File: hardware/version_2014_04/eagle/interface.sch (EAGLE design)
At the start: 19 parts

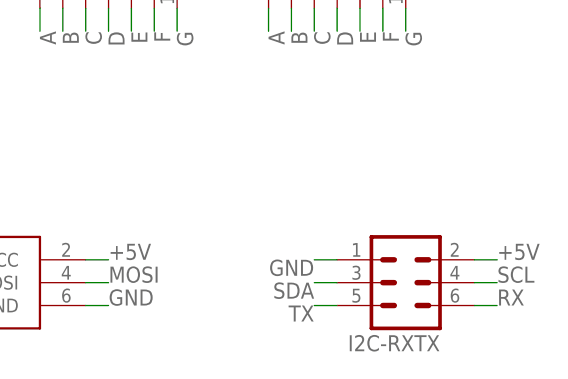
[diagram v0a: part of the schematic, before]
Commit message: mirrored RXTX connector
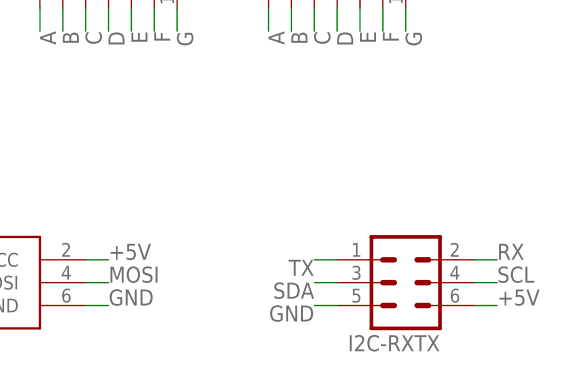
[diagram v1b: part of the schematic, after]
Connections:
- net +5V: now also I2C-RXTX.6; no longer I2C-RXTX.2
- net GND: now also I2C-RXTX.5; no longer I2C-RXTX.1
- net RX: now also I2C-RXTX.2; no longer I2C-RXTX.6
- net TX: now also I2C-RXTX.1; no longer I2C-RXTX.5
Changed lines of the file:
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@@
-</segment>
-<segment>
-<pinref part="I2C-RXTX" gate="1" pin="1"/>
-<wire x1="190.5" y1="15.24" x2="187.96" y2="15.24" width="0.1524" layer="91"/>
-<label x="187.96" y="15.24" size="1.778" layer="95" rot="R180"/>
 </segment>
 <segment>
@@
 <pinref part="C1" gate="G$1" pin="2"/>
 <pinref part="GND3" gate="1" pin="GND"/>
+</segment>
+<segment>
+<pinref part="I2C-RXTX" gate="1" pin="5"/>
+<wire x1="190.5" y1="10.16" x2="187.96" y2="10.16" width="0.1524" layer="91"/>
+<label x="187.96" y="10.16" size="1.778" layer="95" rot="R180"/>
 </segment>
 </net>
@@
 </segment>
 <segment>
-<pinref part="I2C-RXTX" gate="1" pin="2"/>
-<wire x1="205.74" y1="15.24" x2="208.28" y2="15.24" width="0.1524" layer="91"/>
-<label x="208.28" y="15.24" size="1.778" layer="95"/>
-</segment>
-<segment>
 <pinref part="ISP" gate="G$1" pin="VCC"/>
 <wire x1="162.56" y1="15.24" x2="165.1" y2="15.24" width="0.1524" layer="91"/>
@@
 <label x="-15.24" y="68.58" size="1.778" layer="95"/>
 </segment>
+<segment>
+<pinref part="I2C-RXTX" gate="1" pin="6"/>
+<wire x1="205.74" y1="10.16" x2="208.28" y2="10.16" width="0.1524" layer="91"/>
+<label x="208.28" y="10.16" size="1.778" layer="95"/>
+</segment>
 </net>
 <net name="A" class="0">
@@
 </segment>
 <segment>
-<pinref part="I2C-RXTX" gate="1" pin="6"/>
-<wire x1="205.74" y1="10.16" x2="208.28" y2="10.16" width="0.1524" layer="91"/>
-<label x="208.28" y="10.16" size="1.778" layer="95"/>
+<pinref part="I2C-RXTX" gate="1" pin="2"/>
+<wire x1="205.74" y1="15.24" x2="208.28" y2="15.24" width="0.1524" layer="91"/>
+<label x="208.28" y="15.24" size="1.778" layer="95"/>
 </segment>
 </net>
@@
 </segment>
 <segment>
-<pinref part="I2C-RXTX" gate="1" pin="5"/>
-<wire x1="190.5" y1="10.16" x2="187.96" y2="10.16" width="0.1524" layer="91"/>
-<label x="187.96" y="10.16" size="1.778" layer="95" rot="R180"/>
-</segment>
-</net>
+<pinref part="I2C-RXTX" gate="1" pin="1"/>
+<wire x1="190.5" y1="15.24" x2="187.96" y2="15.24" width="0.1524" layer="91"/>
+<label x="187.96" y="15.24" size="1.778" layer="95" rot="R180"/>
+</segment>
+</net>
